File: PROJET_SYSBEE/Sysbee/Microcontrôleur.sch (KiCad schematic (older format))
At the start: 19 parts, among them J7 Connecteur programmation, J8 Micro_SD_Card_Det_Hirose_DM3AT, J9 Conn_01x03, U1 STM32L073CZTx

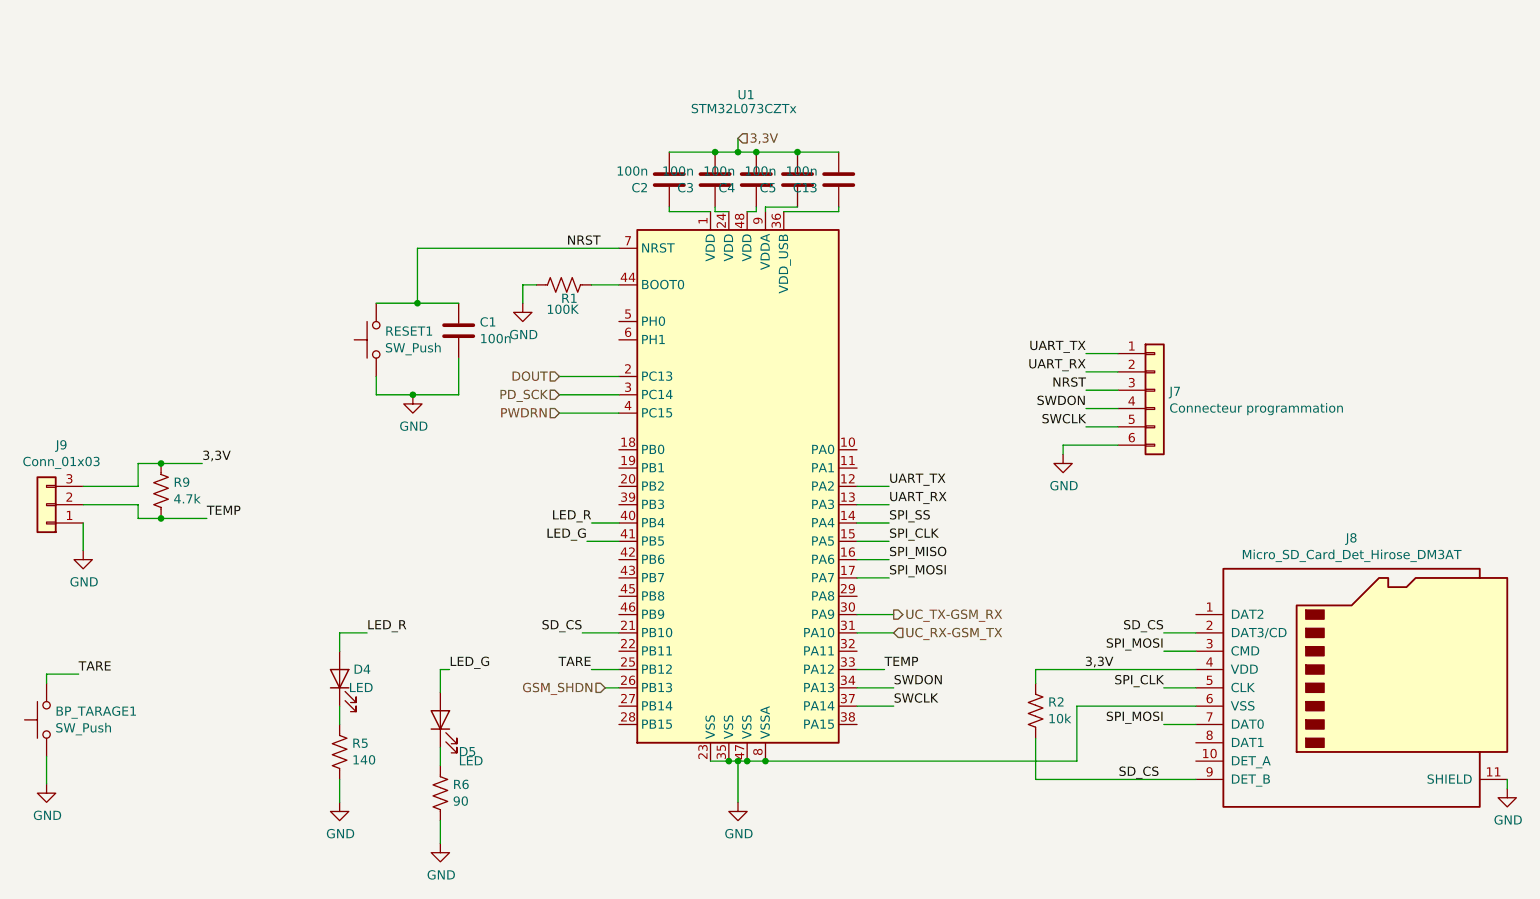
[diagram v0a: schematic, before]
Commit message: placement et routage, reste à redessiner un peu les pistes et rajouter les écritures F.Silks
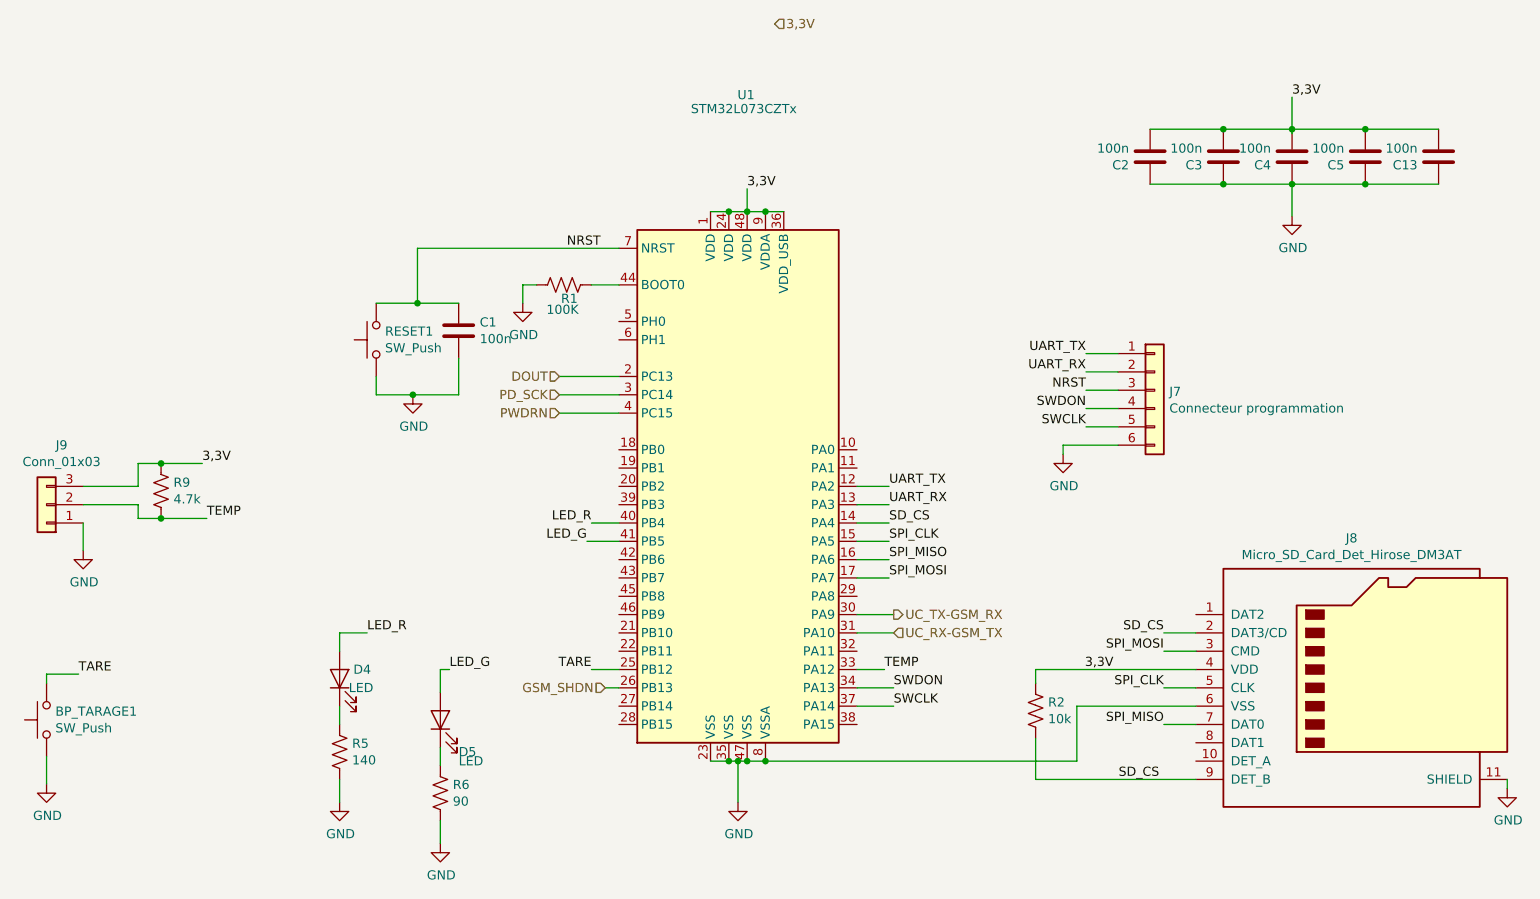
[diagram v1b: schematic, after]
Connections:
- net SPI_SS is gone; now on net SD_CS: U1.14 (PA4)
- net 3,3V: now also U1.1 (VDD), U1.24 (VDD), U1.36 (VDD_USB), U1.48 (VDD), U1.9 (VDDA)
- net GND: now also C13.1, C2.1, C3.1, C4.1, C5.1
- net SD_CS: no longer U1.21 (PB10)
- net SPI_MISO: now also J8.7 (DAT0)
- net SPI_MOSI: no longer J8.7 (DAT0)
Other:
- moved on the sheet: C13, C2, C3, C4, C5
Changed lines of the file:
@@
 L Sysbee-rescue:C-Device C?
 U 1 1 60440282
-P 5725 1900
+P 8825 1775
 AR Path="/60193A3A/60440282" Ref="C?"  Part="1"
 AR Path="/60439374/60440282" Ref="C5"  Part="1"
-F 0 "C5" H 5840 1946 50  0000 L CNN
-F 1 "100n" H 5840 1855 50  0000 L CNN
-F 2 "Capacitor_Tantalum_SMD:CP_EIA-3216-18_Kemet-A" H 5763 1750 50  0001 C CNN
-F 3 "~" H 5725 1900 50  0001 C CNN
-	1    5725 1900
+F 0 "C5" H 8940 1821 50  0000 L CNN
+F 1 "100n" H 8940 1730 50  0000 L CNN
+F 2 "Capacitor_Tantalum_SMD:CP_EIA-3216-18_Kemet-A" H 8863 1625 50  0001 C CNN
+F 3 "~" H 8825 1775 50  0001 C CNN
+	1    8825 1775
 	-1   0    0    1
 $EndComp
@@
 L Sysbee-rescue:C-Device C?
 U 1 1 60440288
-P 5275 1900
+P 8050 1775
 AR Path="/60193A3A/60440288" Ref="C?"  Part="1"
 AR Path="/60439374/60440288" Ref="C3"  Part="1"
-F 0 "C3" H 5390 1946 50  0000 L CNN
-F 1 "100n" H 5390 1855 50  0000 L CNN
-F 2 "Capacitor_Tantalum_SMD:CP_EIA-3216-18_Kemet-A" H 5313 1750 50  0001 C CNN
-F 3 "~" H 5275 1900 50  0001 C CNN
-	1    5275 1900
+F 0 "C3" H 8165 1821 50  0000 L CNN
+F 1 "100n" H 8165 1730 50  0000 L CNN
+F 2 "Capacitor_Tantalum_SMD:CP_EIA-3216-18_Kemet-A" H 8088 1625 50  0001 C CNN
+F 3 "~" H 8050 1775 50  0001 C CNN
+	1    8050 1775
 	-1   0    0    1
 $EndComp
@@
 L Sysbee-rescue:C-Device C?
 U 1 1 6044029B
-P 5025 1900
+P 7650 1775
 AR Path="/60193A3A/6044029B" Ref="C?"  Part="1"
 AR Path="/60439374/6044029B" Ref="C2"  Part="1"
-F 0 "C2" H 5140 1946 50  0000 L CNN
-F 1 "100n" H 5140 1855 50  0000 L CNN
-F 2 "Capacitor_Tantalum_SMD:CP_EIA-3216-18_Kemet-A" H 5063 1750 50  0001 C CNN
-F 3 "~" H 5025 1900 50  0001 C CNN
-	1    5025 1900
+F 0 "C2" H 7765 1821 50  0000 L CNN
+F 1 "100n" H 7765 1730 50  0000 L CNN
+F 2 "Capacitor_Tantalum_SMD:CP_EIA-3216-18_Kemet-A" H 7688 1625 50  0001 C CNN
+F 3 "~" H 7650 1775 50  0001 C CNN
+	1    7650 1775
 	-1   0    0    1
 $EndComp
@@
 	1    0    0    -1
 $EndComp
-Text HLabel 5400 1675 2    50   Input ~ 0
+Text HLabel 5600 1050 2    50   Input ~ 0
 3,3V
 $Comp
@@
 	1    0    0    -1
 $EndComp
-Wire Wire Line
-	5400 1675 5400 1750
 $Comp
 L Sysbee-rescue:R_US-Device R?
@@
 Text HLabel 4675 4675 0    50   Input ~ 0
 GSM_SHDN
-Text Label 4550 4375 2    50   ~ 0
+Text Label 6225 3775 0    50   ~ 0
 SD_CS
 $Comp
@@
 Text Label 6225 3875 0    50   ~ 0
 SPI_CLK
-Text Label 6225 3775 0    50   ~ 0
-SPI_SS
 Wire Wire Line
 	7175 3350 7175 3400
@@
 	4750 4675 4675 4675
 Wire Wire Line
-	4550 4375 4750 4375
-Wire Wire Line
 	6050 4275 6250 4275
 Wire Wire Line
@@
 	1    0    0    -1
 $EndComp
-Text Label 7725 4875 2    50   ~ 0
-SPI_MOSI
 Wire Wire Line
 	7900 4675 7725 4675
 Wire Wire Line
 	7900 4875 7725 4875
-Wire Wire Line
-	5250 5075 5350 5075
-Wire Wire Line
-	5350 5075 5400 5075
-Connection ~ 5350 5075
-Wire Wire Line
-	5400 5075 5450 5075
-Connection ~ 5450 5075
-Wire Wire Line
-	5450 5075 5550 5075
-Wire Wire Line
-	7250 5075 5550 5075
-Connection ~ 5550 5075
-$Comp
-L Sysbee-rescue:STM32L073CZTx-MCU_ST_STM32L0 U?
-U 1 1 604402A8
-P 5450 3575
-AR Path="/60193A3A/604402A8" Ref="U?"  Part="1"
-AR Path="/60439374/604402A8" Ref="U1"  Part="1"
-F 0 "U1" H 5444 5712 50  0000 C CNN
-F 1 "STM32L073CZTx" H 5432 5636 50  0000 C CNN
-F 2 "Package_QFP:LQFP-48_7x7mm_P0.5mm" H 4850 2175 50  0001 R CNN
-F 3 "http://www.st.com/st-web-ui/static/active/en/resource/technical/document/datasheet/DM00141036.pdf" H 5450 3575 50  0001 C CNN
-	1    5450 3575
-	1    0    0    -1
-$EndComp
-Wire Wire Line
-	5350 2075 5275 2075
-Wire Wire Line
-	5025 2075 5250 2075
 $Comp
 L Sysbee-rescue:C-Device C?
 U 1 1 6044028E
-P 5500 1900
+P 8425 1775
 AR Path="/60193A3A/6044028E" Ref="C?"  Part="1"
 AR Path="/60439374/6044028E" Ref="C4"  Part="1"
-F 0 "C4" H 5615 1946 50  0000 L CNN
-F 1 "100n" H 5615 1855 50  0000 L CNN
-F 2 "Capacitor_Tantalum_SMD:CP_EIA-3216-18_Kemet-A" H 5538 1750 50  0001 C CNN
-F 3 "~" H 5500 1900 50  0001 C CNN
-	1    5500 1900
+F 0 "C4" H 8540 1821 50  0000 L CNN
+F 1 "100n" H 8540 1730 50  0000 L CNN
+F 2 "Capacitor_Tantalum_SMD:CP_EIA-3216-18_Kemet-A" H 8463 1625 50  0001 C CNN
+F 3 "~" H 8425 1775 50  0001 C CNN
+	1    8425 1775
 	-1   0    0    1
 $EndComp
-Wire Wire Line
-	5550 2075 5550 2050
-Wire Wire Line
-	5550 2050 5725 2050
 $Comp
 L Sysbee-rescue:C-Device C?
 U 1 1 6044C47E
-P 5950 1900
+P 9225 1775
 AR Path="/60193A3A/6044C47E" Ref="C?"  Part="1"
 AR Path="/60439374/6044C47E" Ref="C13"  Part="1"
-F 0 "C13" H 6065 1946 50  0000 L CNN
-F 1 "100n" H 6065 1855 50  0000 L CNN
-F 2 "Capacitor_Tantalum_SMD:CP_EIA-3216-18_Kemet-A" H 5988 1750 50  0001 C CNN
-F 3 "~" H 5950 1900 50  0001 C CNN
-	1    5950 1900
+F 0 "C13" H 9340 1821 50  0000 L CNN
+F 1 "100n" H 9340 1730 50  0000 L CNN
+F 2 "Capacitor_Tantalum_SMD:CP_EIA-3216-18_Kemet-A" H 9263 1625 50  0001 C CNN
+F 3 "~" H 9225 1775 50  0001 C CNN
+	1    9225 1775
 	-1   0    0    1
 $EndComp
-Wire Wire Line
-	5025 1750 5275 1750
-Connection ~ 5275 1750
-Wire Wire Line
-	5275 1750 5400 1750
-Connection ~ 5500 1750
-Wire Wire Line
-	5500 1750 5725 1750
-Connection ~ 5725 1750
-Wire Wire Line
-	5725 1750 5950 1750
-Wire Wire Line
-	5025 2075 5025 2050
-Wire Wire Line
-	5275 2075 5275 2050
-Wire Wire Line
-	5450 2075 5500 2075
-Wire Wire Line
-	5500 2075 5500 2050
-Wire Wire Line
-	5650 2075 5950 2075
-Wire Wire Line
-	5950 2075 5950 2050
-Connection ~ 5400 1750
-Wire Wire Line
-	5400 1750 5500 1750
 Text Label 7300 2950 2    50   ~ 0
 UART_RX
@@
 Text Label 2500 3750 0    50   ~ 0
 TEMP
+Wire Wire Line
+	7250 5075 5550 5075
+Connection ~ 5550 5075
+Wire Wire Line
+	5450 5075 5550 5075
+Wire Wire Line
+	5400 5075 5450 5075
+Connection ~ 5450 5075
+Wire Wire Line
+	5350 5075 5400 5075
+Wire Wire Line
+	5250 5075 5350 5075
+Connection ~ 5350 5075
+$Comp
+L Sysbee-rescue:STM32L073CZTx-MCU_ST_STM32L0 U?
+U 1 1 604402A8
+P 5450 3575
+AR Path="/60193A3A/604402A8" Ref="U?"  Part="1"
+AR Path="/60439374/604402A8" Ref="U1"  Part="1"
+F 0 "U1" H 5444 5712 50  0000 C CNN
+F 1 "STM32L073CZTx" H 5432 5636 50  0000 C CNN
+F 2 "Package_QFP:LQFP-48_7x7mm_P0.5mm" H 4850 2175 50  0001 R CNN
+F 3 "http://www.st.com/st-web-ui/static/active/en/resource/technical/document/datasheet/DM00141036.pdf" H 5450 3575 50  0001 C CNN
+	1    5450 3575
+	1    0    0    -1
+$EndComp
+Wire Wire Line
+	5250 2075 5350 2075
+Connection ~ 5350 2075
+Wire Wire Line
+	5350 2075 5450 2075
+Connection ~ 5450 2075
+Wire Wire Line
+	5450 2075 5550 2075
+Connection ~ 5550 2075
+Wire Wire Line
+	5550 2075 5650 2075
+Wire Wire Line
+	5450 2075 5450 1950
+Text Label 5450 1950 0    50   ~ 0
+3,3V
+Wire Wire Line
+	7650 1925 8050 1925
+Connection ~ 8050 1925
+Wire Wire Line
+	8050 1925 8425 1925
+Connection ~ 8425 1925
+Wire Wire Line
+	8425 1925 8825 1925
+Connection ~ 8825 1925
+Wire Wire Line
+	8825 1925 9225 1925
+Wire Wire Line
+	7650 1625 8050 1625
+Connection ~ 8050 1625
+Wire Wire Line
+	8050 1625 8425 1625
+Connection ~ 8425 1625
+Wire Wire Line
+	8425 1625 8825 1625
+Connection ~ 8825 1625
+Wire Wire Line
+	8825 1625 9225 1625
+Text Label 8425 1450 0    50   ~ 0
+3,3V
+Wire Wire Line
+	8425 1450 8425 1625
+Wire Wire Line
+	8425 1625 8425 1650
+$Comp
+L Sysbee-rescue:GND-power #PWR?
+U 1 1 604D158F
+P 8425 2100
+AR Path="/60195E38/604D158F" Ref="#PWR?"  Part="1"
+AR Path="/604D158F" Ref="#PWR?"  Part="1"
+AR Path="/60439374/604D158F" Ref="#PWR0104"  Part="1"
+F 0 "#PWR0104" H 8425 1850 50  0001 C CNN
+F 1 "GND" H 8430 1927 50  0000 C CNN
+F 2 "" H 8425 2100 50  0001 C CNN
+F 3 "" H 8425 2100 50  0001 C CNN
+	1    8425 2100
+	1    0    0    -1
+$EndComp
+Wire Wire Line
+	8425 2100 8425 1925
+Text Label 7725 4875 2    50   ~ 0
+SPI_MISO
 $EndSCHEMATC

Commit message: placement et routage ok
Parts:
- J7: value Connecteur programmation -> Conn Prog STLINKV2
- J8: value Micro_SD_Card_Det_Hirose_DM3AT -> Micro_SD
- RESET1: value SW_Push -> Reset
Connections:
- net NRST: now also J7.5 (Pin_5); no longer J7.3 (Pin_3)
- net SWCLK: now also J7.4 (Pin_4); no longer J7.5 (Pin_5)
- net UART_RX: now also J7.1 (Pin_1); no longer J7.2 (Pin_2)
- net UART_TX: now also J7.2 (Pin_2); no longer J7.1 (Pin_1)
- net DOUT renamed ADC_DOUT
- net PD_SCK renamed ADC_CLK
- net PWDRN renamed ADC_PWDRN
- net SWDON renamed SWDIO
- net SWDIO: now also J7.3 (Pin_3); no longer J7.4 (Pin_4)
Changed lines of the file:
@@
 	7250 4775 7250 5075
 Text HLabel 4425 2975 0    50   Input ~ 0
-DOUT
-Text HLabel 4425 3075 0    50   Input ~ 0
-PD_SCK
+ADC_DOUT
+Text HLabel 4425 3075 0    50   Output ~ 0
+ADC_CLK
 Text Label 6225 4075 0    50   ~ 0
 SPI_MOSI
@@
 	1    0    0    -1
 $EndComp
+Text Label 7300 3250 2    50   ~ 0
+NRST
+Text Label 7300 3150 2    50   ~ 0
+SWCLK
 Text Label 7300 3050 2    50   ~ 0
-NRST
-Text Label 7300 3250 2    50   ~ 0
-SWCLK
-Text Label 7300 3150 2    50   ~ 0
-SWDON
+SWDIO
 Wire Wire Line
 	7475 3350 7175 3350
@@
 P 7675 3050
 F 0 "J7" H 7755 3042 50  0000 L CNN
-F 1 "Connecteur programmation" H 7755 2951 50  0000 L CNN
+F 1 "Conn Prog STLINKV2" H 7755 2951 50  0000 L CNN
 F 2 "Micro-match:Micro-match_6" H 7675 3050 50  0001 C CNN
 F 3 "~" H 7675 3050 50  0001 C CNN
@@
 Text Label 6250 4775 0    50   ~ 0
 SWCLK
-Text Label 6250 4675 0    50   ~ 0
-SWDON
 Text Label 7725 4675 2    50   ~ 0
 SPI_CLK
@@
 AR Path="/60439374/603301DD" Ref="J8"  Part="1"
 F 0 "J8" H 8750 5492 50  0000 C CNN
-F 1 "Micro_SD_Card_Det_Hirose_DM3AT" H 8750 5401 50  0000 C CNN
+F 1 "Micro_SD" H 8750 5401 50  0000 C CNN
 F 2 "Connector_Card:microSD_HC_Molex_104031-0811" H 10850 5375 50  0001 C CNN
 F 3 "" H 8800 4775 50  0001 C CNN
@@
 	-1   0    0    1
 $EndComp
+Text Label 7300 2850 2    50   ~ 0
+UART_RX
 Text Label 7300 2950 2    50   ~ 0
-UART_RX
-Text Label 7300 2850 2    50   ~ 0
 UART_TX
 Wire Wire Line
 	4750 3175 4425 3175
-Text HLabel 4425 3175 0    50   Input ~ 0
-PWDRN
+Text HLabel 4425 3175 0    50   Output ~ 0
+ADC_PWDRN
 Text Label 4650 2275 2    50   ~ 0
 NRST
@@
 AR Path="/60439374/604402AE" Ref="RESET1"  Part="1"
 F 0 "RESET1" V 3471 2727 50  0000 R CNN
-F 1 "SW_Push" V 3380 2727 50  0000 R CNN
+F 1 "Reset" V 3380 2727 50  0000 R CNN
 F 2 "Button_Switch_SMD:SW_SPST_TL3305C" H 3425 2975 50  0001 C CNN
 F 3 "~" H 3425 2975 50  0001 C CNN
@@
 Text Label 7725 4875 2    50   ~ 0
 SPI_MISO
+Text Label 6250 4675 0    50   ~ 0
+SWDIO
 $EndSCHEMATC
